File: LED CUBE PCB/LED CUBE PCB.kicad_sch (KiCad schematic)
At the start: 0 parts

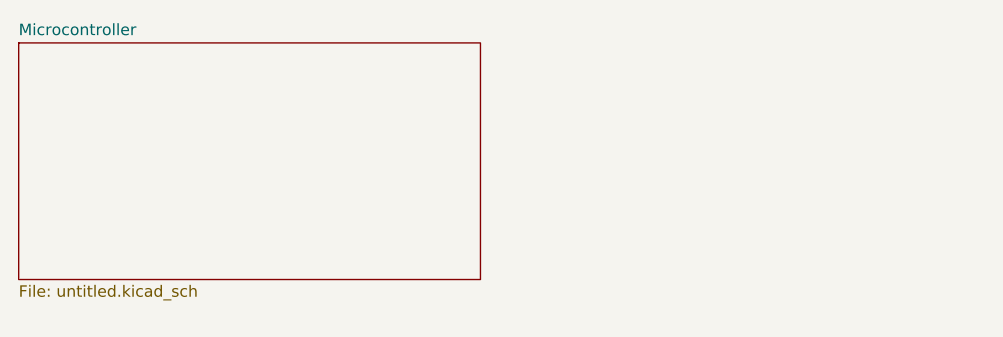
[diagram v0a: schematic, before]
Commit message: Added logic level converter
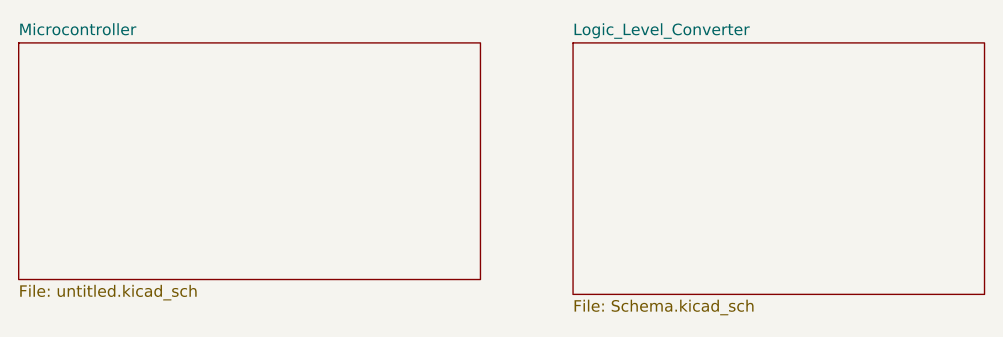
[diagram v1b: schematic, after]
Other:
- added sheet Logic_Level_Converter (Schema.kicad_sch)
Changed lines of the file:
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@@
+    )
+  )
+  (sheet (at 97.79 27.94) (size 45.72 27.94) (fields_autoplaced)
+    (stroke (width 0.1524) (type solid))
+    (fill (color 0 0 0 0.0000))
+    (property "Sheetname" "Logic_Level_Converter" (at 97.79 27.2284 0)
+      (effects (font (size 1.27 1.27)) (justify left bottom))
+    )
+    (property "Sheetfile" "Schema.kicad_sch" (at 97.79 56.4646 0)
+      (effects (font (size 1.27 1.27)) (justify left top))
+    )
+    (instances
+      (project "LED CUBE PCB"
+        (path "/64eb2d32-222b-4351-90b6-2cc90b760e62" (page "3"))
+      )
     )
   )
